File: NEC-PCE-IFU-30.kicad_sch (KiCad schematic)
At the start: 0 parts

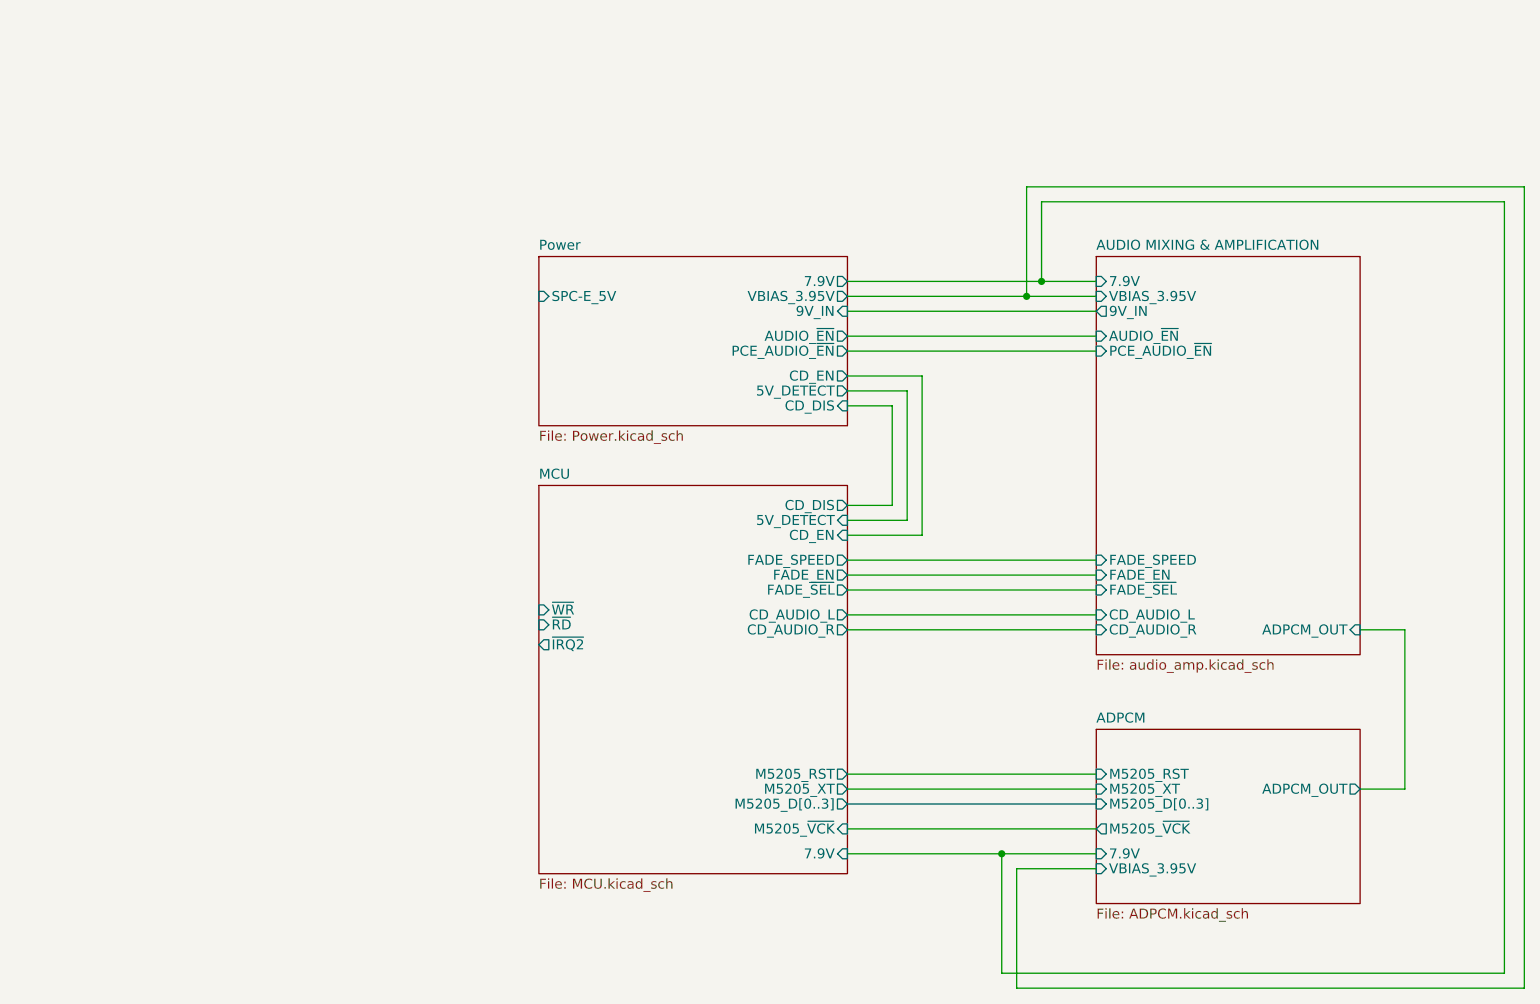
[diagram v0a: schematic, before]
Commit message: PCE expansion port added with only relevant pins.
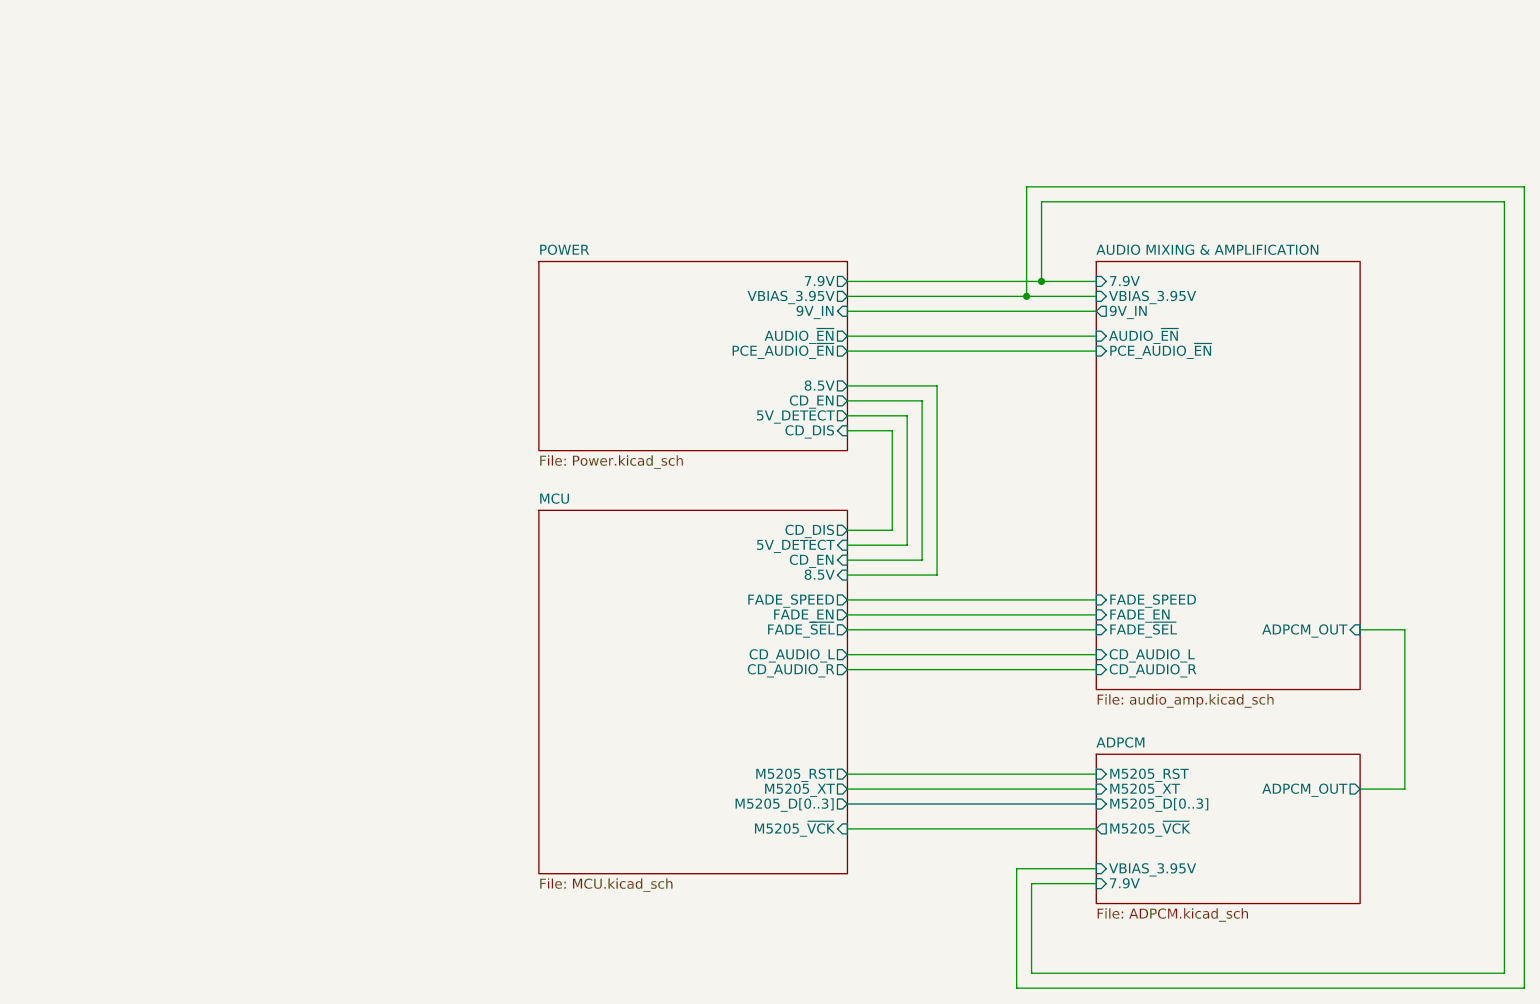
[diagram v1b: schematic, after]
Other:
- sheet Power renamed POWER
- sheet MCU ports: added 8.5V; removed 7.9V, ~{IRQ2}, ~{RD}, ~{WR}
- sheet POWER ports: added 8.5V; removed SPC-E_5V

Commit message: All calculations added.
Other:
- sheet ADPCM ports: added none; removed 7.9V
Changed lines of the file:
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@@
   (junction (at 154.305 56.515) (diameter 0) (color 0 0 0 0)
   )
-  (junction (at 156.21 54.61) (diameter 0) (color 0 0 0 0)
-  )
   (wire (pts (xy 131.445 117.475) (xy 163.195 117.475))
     (stroke (width 0) (type default) (color 0 0 0 0))
@@
     (stroke (width 0) (type default) (color 0 0 0 0))
   )
-  (wire (pts (xy 156.21 54.61) (xy 163.195 54.61))
-    (stroke (width 0) (type default) (color 0 0 0 0))
-  )
   (wire (pts (xy 140.97 69.85) (xy 140.97 90.17))
     (stroke (width 0) (type default) (color 0 0 0 0))
   )
-  (wire (pts (xy 131.445 54.61) (xy 156.21 54.61))
+  (wire (pts (xy 131.445 54.61) (xy 163.195 54.61))
     (stroke (width 0) (type default) (color 0 0 0 0))
   )
@@
     (stroke (width 0) (type default) (color 0 0 0 0))
   )
-  (wire (pts (xy 154.94 142.875) (xy 154.94 131.445))
-    (stroke (width 0) (type default) (color 0 0 0 0))
-  )
-  (wire (pts (xy 156.21 44.45) (xy 156.21 54.61))
-    (stroke (width 0) (type default) (color 0 0 0 0))
-  )
-  (wire (pts (xy 154.94 131.445) (xy 163.195 131.445))
-    (stroke (width 0) (type default) (color 0 0 0 0))
-  )
   (wire (pts (xy 217.805 144.78) (xy 153.035 144.78))
     (stroke (width 0) (type default) (color 0 0 0 0))
   )
-  (wire (pts (xy 215.265 142.875) (xy 154.94 142.875))
-    (stroke (width 0) (type default) (color 0 0 0 0))
-  )
   (wire (pts (xy 154.305 56.515) (xy 154.305 42.545))
     (stroke (width 0) (type default) (color 0 0 0 0))
@@
     (stroke (width 0) (type default) (color 0 0 0 0))
   )
-  (wire (pts (xy 156.21 44.45) (xy 215.265 44.45))
-    (stroke (width 0) (type default) (color 0 0 0 0))
-  )
   (wire (pts (xy 131.445 104.14) (xy 163.195 104.14))
     (stroke (width 0) (type default) (color 0 0 0 0))
@@
   )
   (wire (pts (xy 142.875 67.945) (xy 142.875 92.075))
-    (stroke (width 0) (type default) (color 0 0 0 0))
-  )
-  (wire (pts (xy 215.265 44.45) (xy 215.265 142.875))
     (stroke (width 0) (type default) (color 0 0 0 0))
   )
@@
     (property "Sheet file" "ADPCM.kicad_sch" (id 1) (at 163.195 134.5696 0)
       (effects (font (size 1.27 1.27)) (justify left top))
-    )
-    (pin "7.9V" input (at 163.195 131.445 180)
-      (effects (font (size 1.27 1.27)) (justify left))
     )
     (pin "M5205_~{VCK}" output (at 163.195 124.46 180)
@@
       (reference "#PWR0101") (unit 1) (value "GND") (footprint "")
     )
-    (path "/6773dc59-1a0f-4ef1-9716-1306879c4c35/f2bf42bc-c782-4848-98ad-6b33890eb90a"
+    (path "/0578f93e-ca38-43d5-ab59-174de13ad696/fb0a236e-2959-4c40-af42-baa3789a9a70"
       (reference "#PWR0102") (unit 1) (value "GND") (footprint "")
     )
@@
       (reference "IC114") (unit 2) (value "TL072") (footprint "")
     )
-    (path "/6773dc59-1a0f-4ef1-9716-1306879c4c35/924baf15-b9fe-4ca0-aad7-35c9e8ecc6cb"
+    (path "/0578f93e-ca38-43d5-ab59-174de13ad696/54756e58-219f-4927-8acd-8cfa5ff6b217"
       (reference "IC114") (unit 3) (value "TL072") (footprint "")
     )
@@
     )
     (path "/d1484c84-275c-4498-a17e-3c62a3d51fc3/3ba36b0d-fb43-483a-9757-03e73bb0e033"
-      (reference "R91") (unit 1) (value "82k") (footprint "")
+      (reference "R91") (unit 1) (value "8.2k") (footprint "")
     )
     (path "/d1484c84-275c-4498-a17e-3c62a3d51fc3/52d59f57-e0f9-44e6-a8d5-c7e7a1797d10"
-      (reference "R92") (unit 1) (value "82k") (footprint "")
+      (reference "R92") (unit 1) (value "8.2k") (footprint "")
     )
     (path "/d1484c84-275c-4498-a17e-3c62a3d51fc3/1a3933e7-9660-4398-ba84-b5d283b5c133"

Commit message: Documentation update
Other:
- sheet ADPCM ports: added VBIAS_3.9V; removed VBIAS_3.95V
- sheet AUDIO MIXING & AMPLIFICATION ports: added 7.8V, VBIAS_3.9V; removed 7.9V, VBIAS_3.95V
- sheet POWER ports: added 7.8V, VBIAS_3.9V; removed 7.9V, VBIAS_3.95V
- note added: "Note on transistors: A1175 = PNP A144 = PNP C2001 = NPN AIL3Z = NPN C2785 = NPN External mod on PCB R999, 2k2"

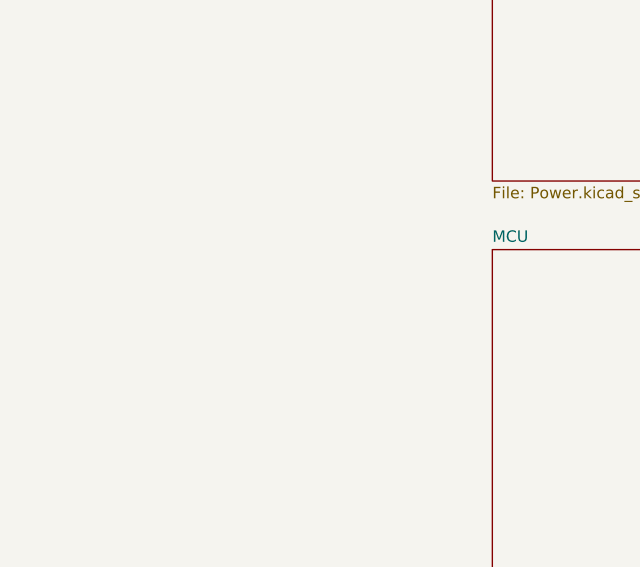
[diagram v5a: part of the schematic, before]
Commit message: Unsused pins from expansion conenctor on 1 page. CD conenctor signals added.
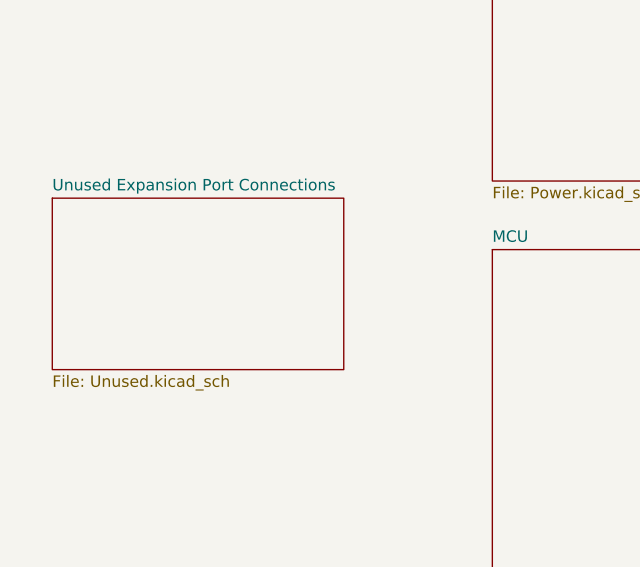
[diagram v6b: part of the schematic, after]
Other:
- added sheet Unused Expansion Port Connections (Unused.kicad_sch)
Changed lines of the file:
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@@
+    )
+  )
+  (sheet (at 43.18 78.105) (size 32.385 19.05) (fields_autoplaced)
+    (stroke (width 0.1524) (type solid) (color 0 0 0 0))
+    (fill (color 0 0 0 0.0000))
+    (property "Sheet name" "Unused Expansion Port Connections" (id 0) (at 43.18 77.3934 0)
+      (effects (font (size 1.27 1.27)) (justify left bottom))
+    )
+    (property "Sheet file" "Unused.kicad_sch" (id 1) (at 43.18 97.7396 0)
+      (effects (font (size 1.27 1.27)) (justify left top))
     )
   )
@@
     (path "/0578f93e-ca38-43d5-ab59-174de13ad696" (page "4"))
     (path "/d1484c84-275c-4498-a17e-3c62a3d51fc3" (page "5"))
+    (path "/86a71b1a-8204-43be-a56e-bd6873a052ba" (page "6"))
   )
   (symbol_instances
@@
       (reference "#PWR0225") (unit 1) (value "GND") (footprint "")
     )
+    (path "/16ed6a89-2253-4800-b858-7195f8e7cad5/b0219956-d897-442f-9032-332e90d7c3f8"
+      (reference "#PWR0226") (unit 1) (value "GND") (footprint "")
+    )
     (path "/d1484c84-275c-4498-a17e-3c62a3d51fc3/97a504e3-b65a-4f55-a0f0-08565693b9e7"
-      (reference "#PWR?") (unit 1) (value "GND") (footprint "")
+      (reference "#PWR0227") (unit 1) (value "GND") (footprint "")
     )
     (path "/16ed6a89-2253-4800-b858-7195f8e7cad5/e579e631-d771-4c4e-8737-93216687f533"
@@
       (reference "SPC-E1") (unit 4) (value "PCE-EXPANSION-CONN") (footprint "")
     )
+    (path "/86a71b1a-8204-43be-a56e-bd6873a052ba/19f8b08c-3293-427c-9636-e5c2aa2e68b8"
+      (reference "SPC-E1") (unit 5) (value "PCE-EXPANSION-CONN") (footprint "")
+    )
     (path "/0578f93e-ca38-43d5-ab59-174de13ad696/295c8cb7-bc56-4176-ae26-34755bafa866"

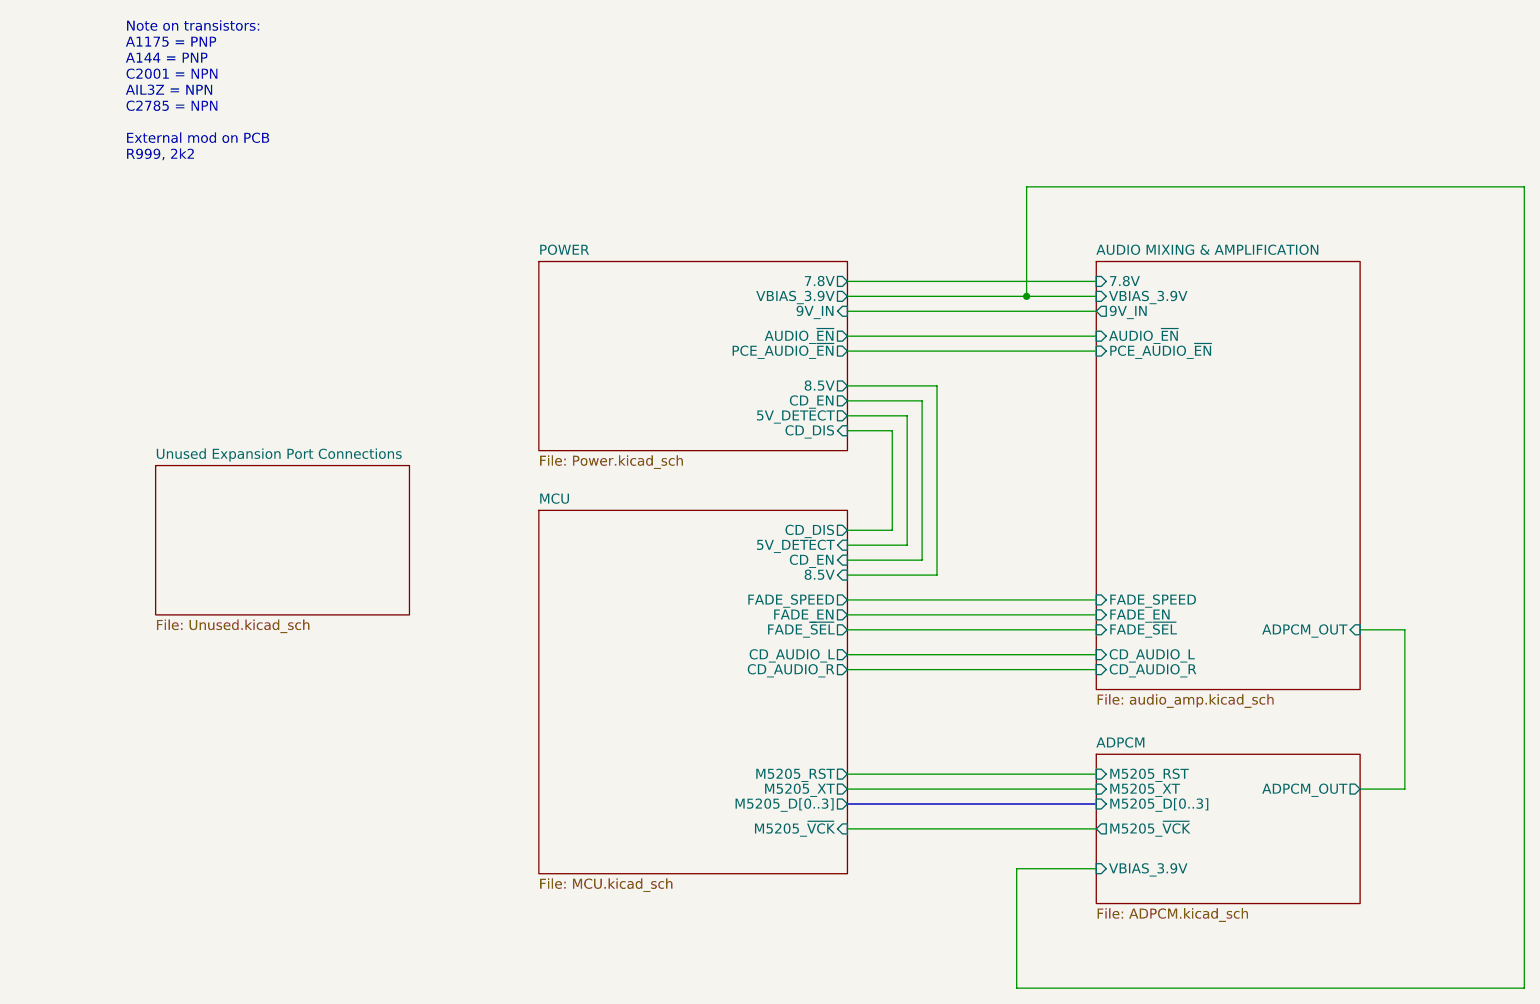
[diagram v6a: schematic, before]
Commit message: Fixed a few typos and mainly renamed connections to CD-ROM with more accurate descriptions
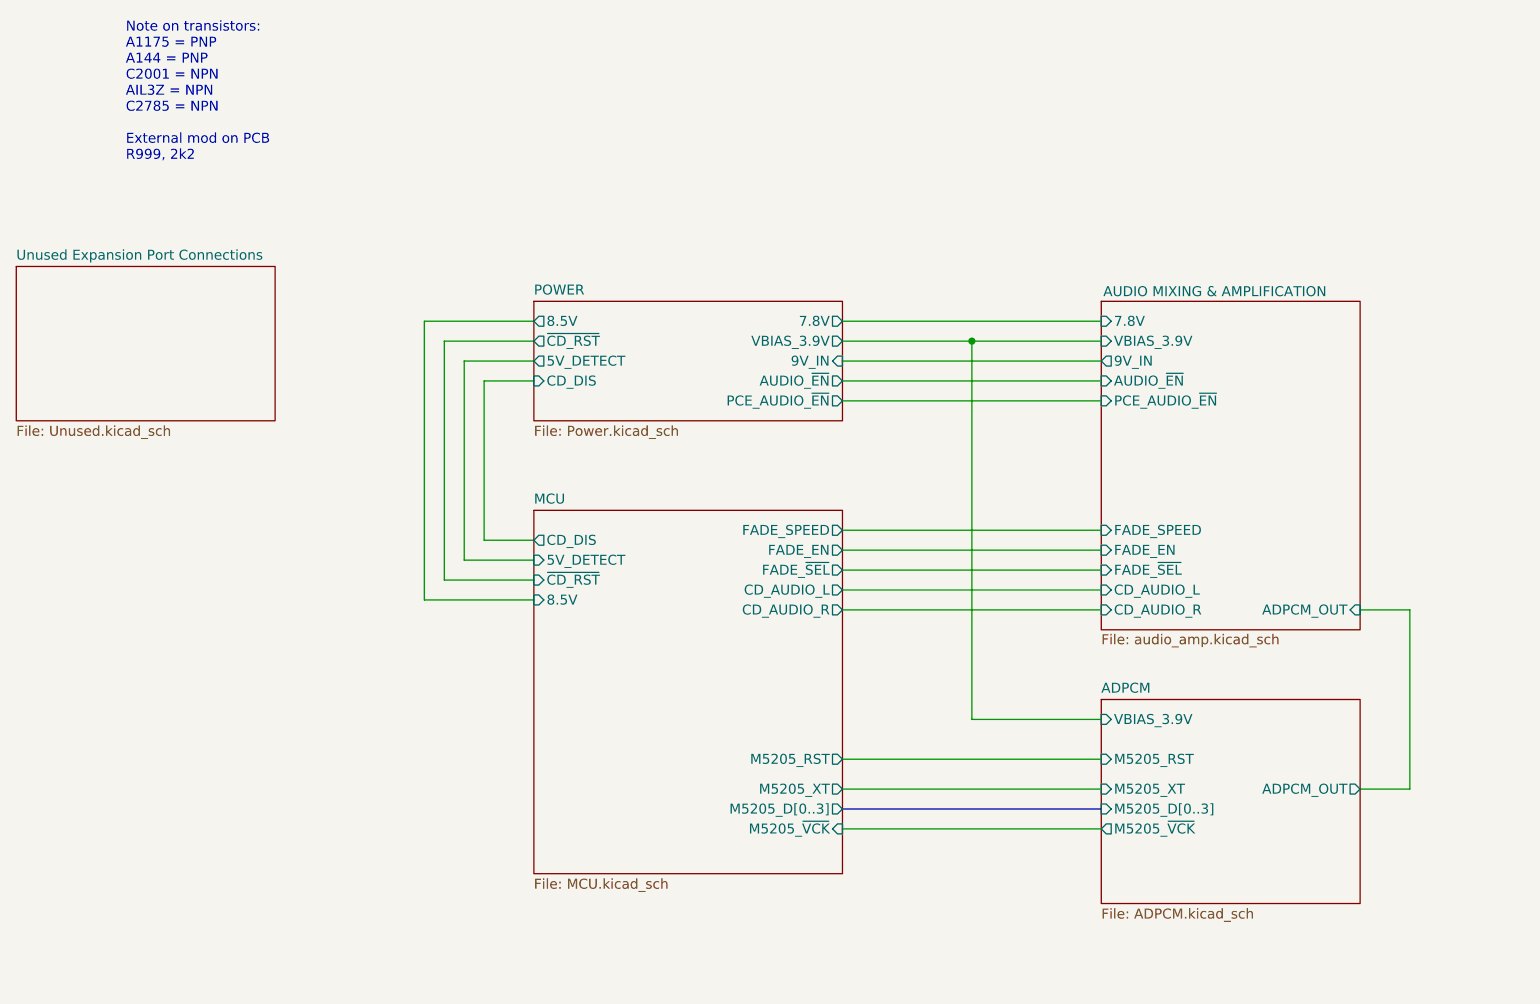
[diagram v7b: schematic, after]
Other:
- sheet MCU ports: added ~{CD_RST}; removed CD_EN
- sheet POWER ports: added ~{CD_RST}; removed CD_EN
